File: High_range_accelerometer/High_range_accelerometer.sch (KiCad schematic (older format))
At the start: 56 parts, among them J1 USB_B_Micro, P1 KRC_PSoCWriter, U1 KRC_Conn_CAN, U2 LT1965xDD-3.3, U3 LT1761-5, U4 NCV7342, U5 CY8C5868LTI-LP039, U6 H3LIS331DLTR, U7 W25N01GVxxIG-IT, Y1 Crystal_kHz, Y2 Crystal_MHz

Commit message: とりあえずできた
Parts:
- removed C21, C22: 9pF, Capacitor_SMD:C_0201_0603Metric, symbol Device:C_Small
- removed Y1: Crystal_kHz, KUTKiCad_footprint:Crystal_SeikoEpson_FC-135, symbol Device:Crystal
- C10, C12, C13, C15, C17, C20, C23, C24, C25, C27, C4, C7, C8, C9: footprint Capacitor_SMD:C_0201_0603Metric -> Capacitor_SMD:C_0402_1005Metric
- C11, C14, C16, C18, C19, C2: footprint Capacitor_SMD:C_0603_1608Metric -> Capacitor_SMD:C_0402_1005Metric
- J1: footprint Connector_USB:USB_Micro-B_Amphenol_10103594-0001LF_Horizontal -> KUTKiCad_footprint:Hirose_ZX_ZX62D-B-5P8
- P1: symbol KUT_Connector:KRC_PSoCWriter -> High_range_accelerometer-rescue:KRC_PSoCWriter-KUT_Connector
- R10, R11, R2, R3, R4, R5, R6, R7, R8, R9: footprint Resistor_SMD:R_0603_1608Metric -> Capacitor_SMD:C_0402_1005Metric
- U5: footprint Package_DFN_QFN:QFN-68-1EP_8x8mm_P0.4mm_EP5.2x5.2mm_ThermalVias -> KUTKiCad_footprint:Cypress_QFN-68_EP_8x8_Pitch0.4mm
- U6: symbol My_Library:H3LIS331DLTR -> High_range_accelerometer-rescue:H3LIS331DLTR-My_Library
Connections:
- net labels added: LED_G_1, LED_G_2
- wire segments 278 -> 270
- no-connect marks 31 -> 30

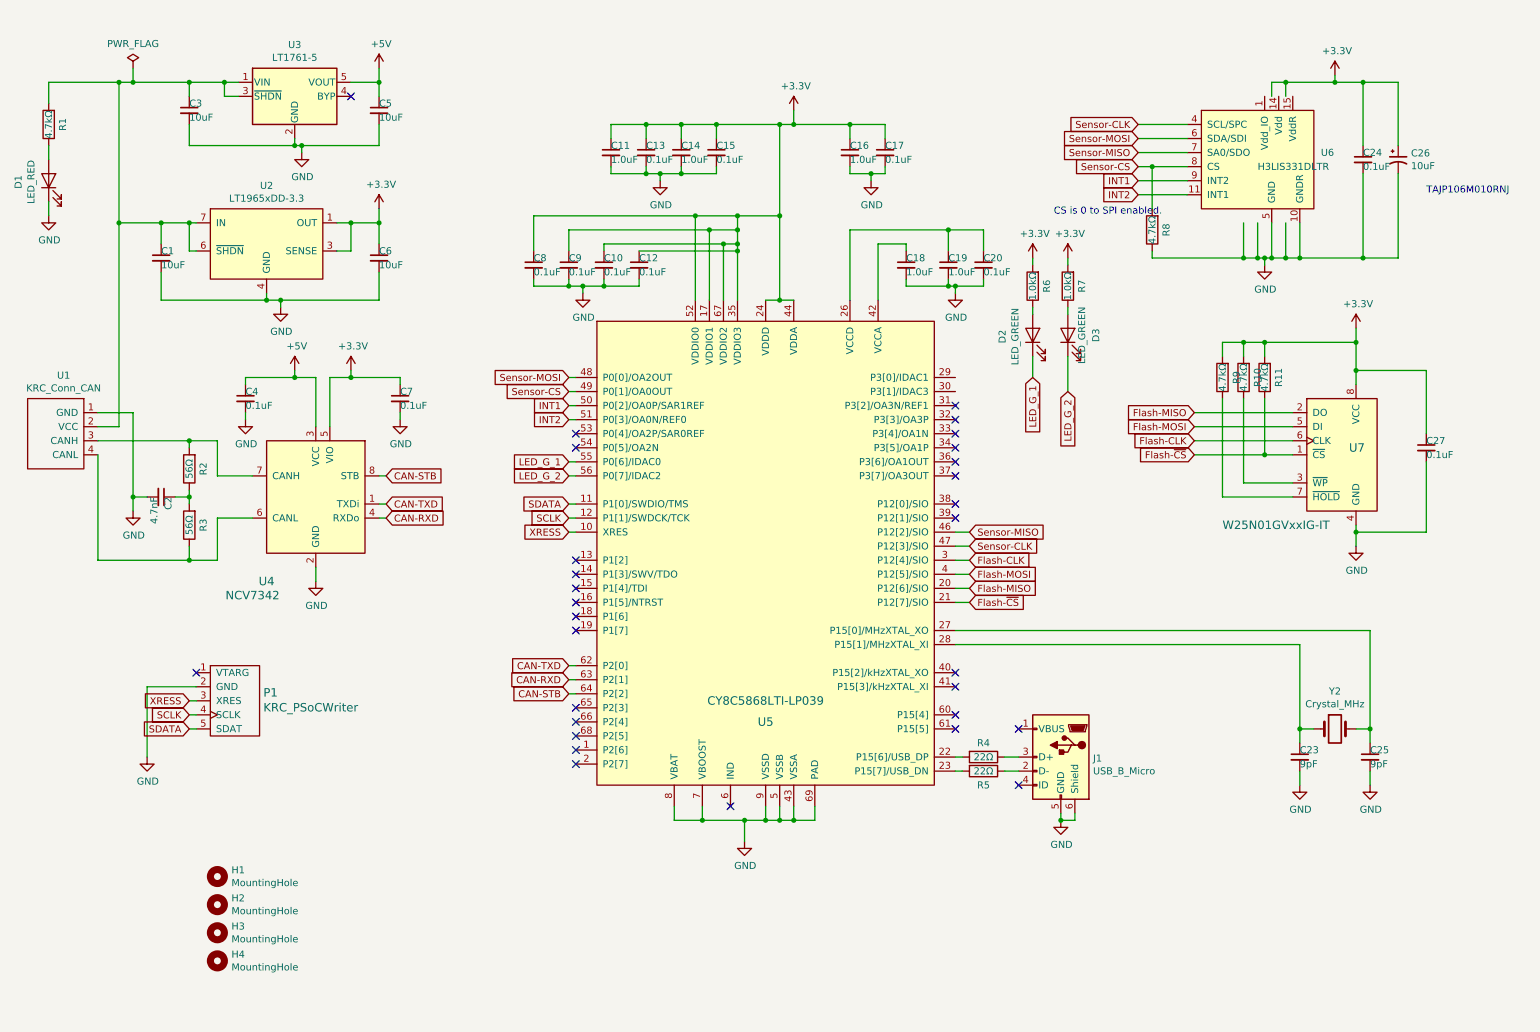
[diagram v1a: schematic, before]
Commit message: change regulator
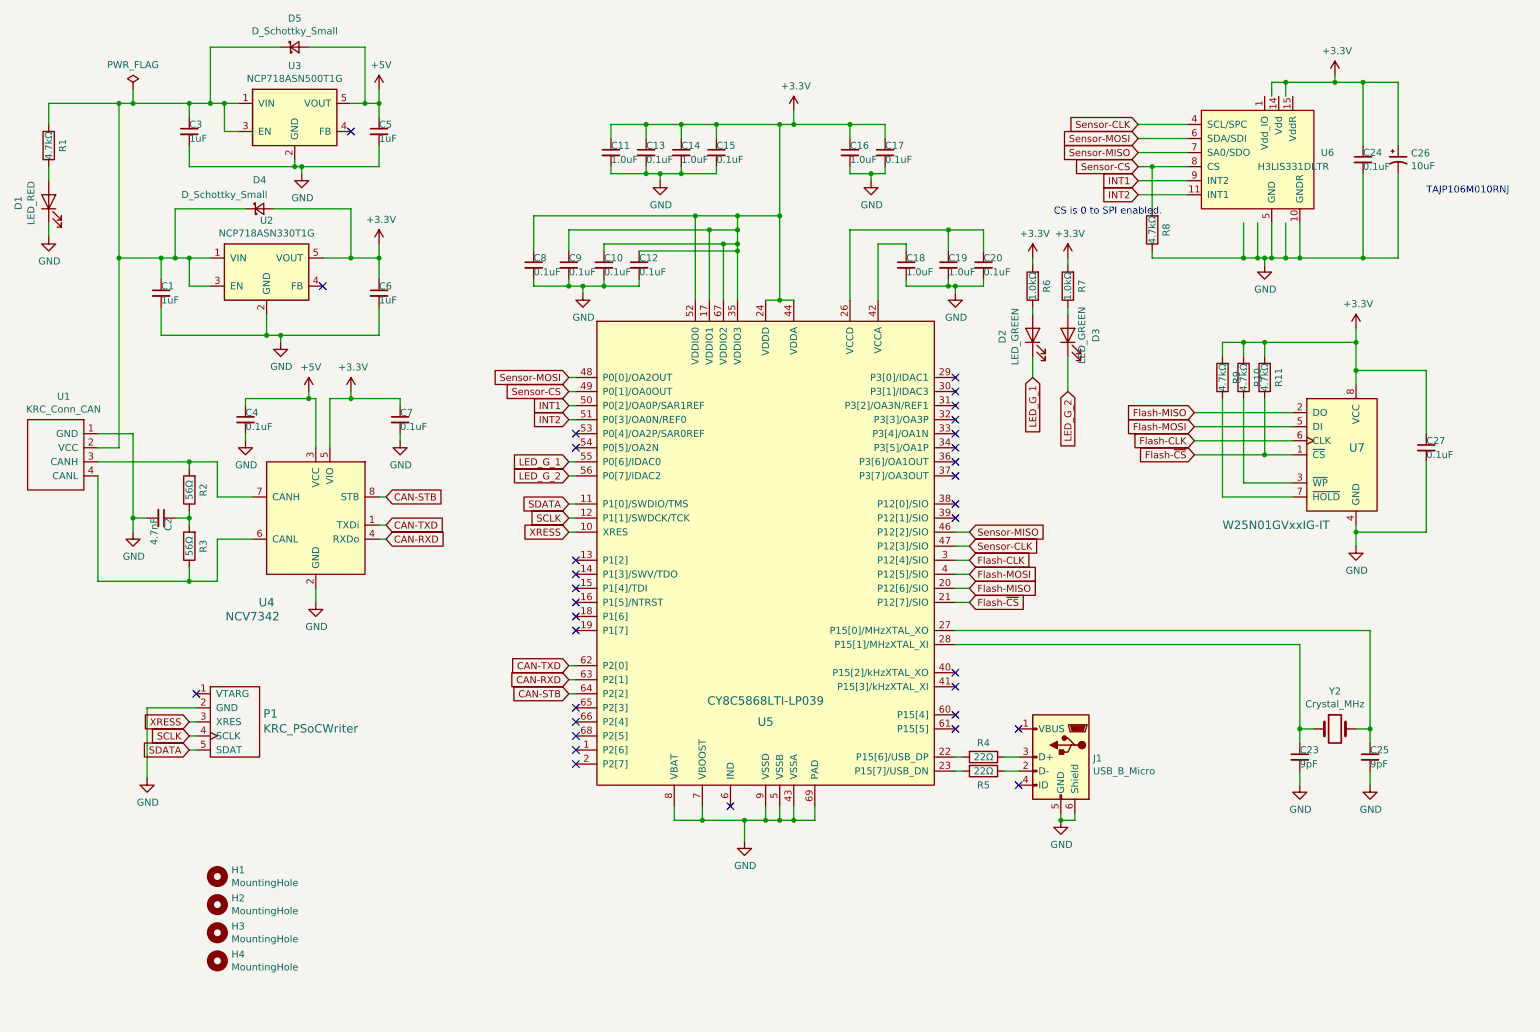
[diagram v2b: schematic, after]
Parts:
- removed U2: LT1965xDD-3.3, KUTKiCad_footprint:DFN-8-1EP_3x3mm_P0.65mm_EP1.7x2.56mm, symbol KUTKiCad_symbol:LT1965xDD-3.3
- removed U3: LT1761-5, Package_TO_SOT_SMD:TSOT-23-5, symbol Regulator_Linear:LT1761-5
- added D4, D5: D_Schottky_Small, Diode_SMD:D_0603_1608Metric, symbol Device:D_Schottky_Small
- added U2: NCP718ASN330T1G, Package_TO_SOT_SMD:TSOT-23-5, symbol Regulator_Linear:ADP7142AUZJ
- added U3: NCP718ASN500T1G, Package_TO_SOT_SMD:TSOT-23-5, symbol Regulator_Linear:ADP7142AUZJ
- C1, C3, C5, C6: value 10uF -> 1uF; footprint Capacitor_SMD:C_0603_1608Metric -> Capacitor_SMD:C_0402_1005Metric
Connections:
- net +3V3: now also D4.2 (A), U2.5 (VOUT)
- net +5V: now also D5.2 (A), U3.5 (VOUT)
- net GND: now also U2.2 (GND), U3.2 (GND)
- net at C1.1, C3.1, R1.2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: now also D4.1 (K), D5.1 (K), U2.1 (VIN), U2.3 (EN), U3.1 (VIN), U3.3 (EN)
- no-connect marks 30 -> 33
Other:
- moved on the sheet: C1, C2, C3, C4, C5, C6, C7, D1, P1, R1, R2, R3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

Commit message: add SVG and PDF and Gerber files
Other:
- moved on the sheet: H1, H2, H3, H4, P1
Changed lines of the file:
@@
 L High_range_accelerometer-rescue:KRC_PSoCWriter-KUT_Connector P1
 U 1 1 5D89CA7D
-P 2100 5500
-F 0 "P1" H 2377 5558 60  0000 L CNN
-F 1 "KRC_PSoCWriter" H 2377 5452 60  0000 L CNN
-F 2 "KUTKiCad_footprint:JST_JQ_05JQ-BT_1x05_P2.5mm_Vertical" H 2325 5500 60  0001 C CNN
-F 3 "" H 2325 5500 60  0000 C CNN
-	1    2100 5500
+P 2200 5200
+F 0 "P1" H 2477 5258 60  0000 L CNN
+F 1 "KRC_PSoCWriter" H 2477 5152 60  0000 L CNN
+F 2 "KUTKiCad_footprint:JST_JQ_05JQ-BT_1x05_P2.5mm_Vertical" H 2425 5200 60  0001 C CNN
+F 3 "" H 2425 5200 60  0000 C CNN
+	1    2200 5200
 	1    0    0    -1
 $EndComp
@@
 L power:GND #PWR03
 U 1 1 5D8A2416
-P 1550 5900
-F 0 "#PWR03" H 1550 5650 50  0001 C CNN
-F 1 "GND" H 1555 5727 50  0000 C CNN
-F 2 "" H 1550 5900 50  0001 C CNN
-F 3 "" H 1550 5900 50  0001 C CNN
-	1    1550 5900
-	1    0    0    -1
-$EndComp
-Wire Wire Line
-	1550 5900 1550 5400
-Wire Wire Line
-	1550 5400 1900 5400
-Text GLabel 1850 5500 0    50   Input ~ 0
+P 1650 5600
+F 0 "#PWR03" H 1650 5350 50  0001 C CNN
+F 1 "GND" H 1655 5427 50  0000 C CNN
+F 2 "" H 1650 5600 50  0001 C CNN
+F 3 "" H 1650 5600 50  0001 C CNN
+	1    1650 5600
+	1    0    0    -1
+$EndComp
+Wire Wire Line
+	1650 5600 1650 5100
+Wire Wire Line
+	1650 5100 2000 5100
+Text GLabel 1950 5200 0    50   Input ~ 0
 XRESS
-Text GLabel 1850 5600 0    50   Input ~ 0
+Text GLabel 1950 5300 0    50   Input ~ 0
 SCLK
-Text GLabel 1850 5700 0    50   Input ~ 0
+Text GLabel 1950 5400 0    50   Input ~ 0
 SDATA
 Wire Wire Line
-	1850 5700 1900 5700
-Wire Wire Line
-	1900 5600 1850 5600
-Wire Wire Line
-	1850 5500 1900 5500
+	1950 5400 2000 5400
+Wire Wire Line
+	2000 5300 1950 5300
+Wire Wire Line
+	1950 5200 2000 5200
 Text GLabel 4550 4150 0    50   Input ~ 0
 XRESS
@@
 Wire Wire Line
 	3250 4200 3200 4200
-NoConn ~ 1900 5300
+NoConn ~ 2000 5000
 $Comp
 L Device:Crystal Y2
@@
 L Mechanical:MountingHole H1
 U 1 1 5D9A09FB
-P 2050 6600
-F 0 "H1" H 2150 6646 50  0000 L CNN
-F 1 "MountingHole" H 2150 6555 50  0000 L CNN
-F 2 "MountingHole:MountingHole_3.2mm_M3" H 2050 6600 50  0001 C CNN
-F 3 "~" H 2050 6600 50  0001 C CNN
-	1    2050 6600
+P 700 5000
+F 0 "H1" H 800 5046 50  0000 L CNN
+F 1 "MountingHole" H 800 4955 50  0000 L CNN
+F 2 "MountingHole:MountingHole_3.2mm_M3" H 700 5000 50  0001 C CNN
+F 3 "~" H 700 5000 50  0001 C CNN
+	1    700  5000
 	1    0    0    -1
 $EndComp
@@
 L Mechanical:MountingHole H2
 U 1 1 5D9A0A93
-P 2050 6800
-F 0 "H2" H 2150 6846 50  0000 L CNN
-F 1 "MountingHole" H 2150 6755 50  0000 L CNN
-F 2 "MountingHole:MountingHole_3.2mm_M3" H 2050 6800 50  0001 C CNN
-F 3 "~" H 2050 6800 50  0001 C CNN
-	1    2050 6800
+P 700 5200
+F 0 "H2" H 800 5246 50  0000 L CNN
+F 1 "MountingHole" H 800 5155 50  0000 L CNN
+F 2 "MountingHole:MountingHole_3.2mm_M3" H 700 5200 50  0001 C CNN
+F 3 "~" H 700 5200 50  0001 C CNN
+	1    700  5200
 	1    0    0    -1
 $EndComp
@@
 L Mechanical:MountingHole H3
 U 1 1 5D9A0B13
-P 2050 7000
-F 0 "H3" H 2150 7046 50  0000 L CNN
-F 1 "MountingHole" H 2150 6955 50  0000 L CNN
-F 2 "MountingHole:MountingHole_3.2mm_M3" H 2050 7000 50  0001 C CNN
-F 3 "~" H 2050 7000 50  0001 C CNN
-	1    2050 7000
+P 700 5400
+F 0 "H3" H 800 5446 50  0000 L CNN
+F 1 "MountingHole" H 800 5355 50  0000 L CNN
+F 2 "MountingHole:MountingHole_3.2mm_M3" H 700 5400 50  0001 C CNN
+F 3 "~" H 700 5400 50  0001 C CNN
+	1    700  5400
 	1    0    0    -1
 $EndComp
@@
 L Mechanical:MountingHole H4
 U 1 1 5D9A0B95
-P 2050 7200
-F 0 "H4" H 2150 7246 50  0000 L CNN
-F 1 "MountingHole" H 2150 7155 50  0000 L CNN
-F 2 "MountingHole:MountingHole_3.2mm_M3" H 2050 7200 50  0001 C CNN
-F 3 "~" H 2050 7200 50  0001 C CNN
-	1    2050 7200
-	1    0    0    -1
-$EndComp
+P 700 5600
+F 0 "H4" H 800 5646 50  0000 L CNN
+F 1 "MountingHole" H 800 5555 50  0000 L CNN
+F 2 "MountingHole:MountingHole_3.2mm_M3" H 700 5600 50  0001 C CNN
+F 3 "~" H 700 5600 50  0001 C CNN
+	1    700  5600
+	1    0    0    -1
+$EndComp
